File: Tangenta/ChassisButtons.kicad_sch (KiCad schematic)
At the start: 10 parts, among them J2 Conn_02x02_Top_Bottom, U5 74HC74D,653, U6 CD4060SA_TR, U7 74HC04D,653

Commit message: Current progress, power supply.
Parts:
- added Q1, Q2: 2N7002, NMOS_2N7002:NMOS_2N7002, symbol NMOS_2N7002:2N7002
- added R10, R6, R9: 100, Resistor_SMD:R_0603_1608Metric, symbol Device:R_Small_US
- added R7, R8: 10k, Resistor_SMD:R_0603_1608Metric, symbol Device:R_Small_US
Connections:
- net CONN_3: now also R6.1, R7.1
- net GNDREF: now also Q1.2 (S), Q2.2 (S), R7.2, R8.2
- net PS_ON: now also R10.1
- net CONN_4: now reaches U5.5 (1Q)
- net CONN_4: now also Q2.3 (D), R8.1, R9.1
- new net: Q2.1 (G), R6.2
- new net: Q1.3 (D), R10.2
- new net: Q1.1 (G), R9.2
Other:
- moved on the sheet: C1, J2, R1, R2, R3, R4, R5, U5, U6, U7

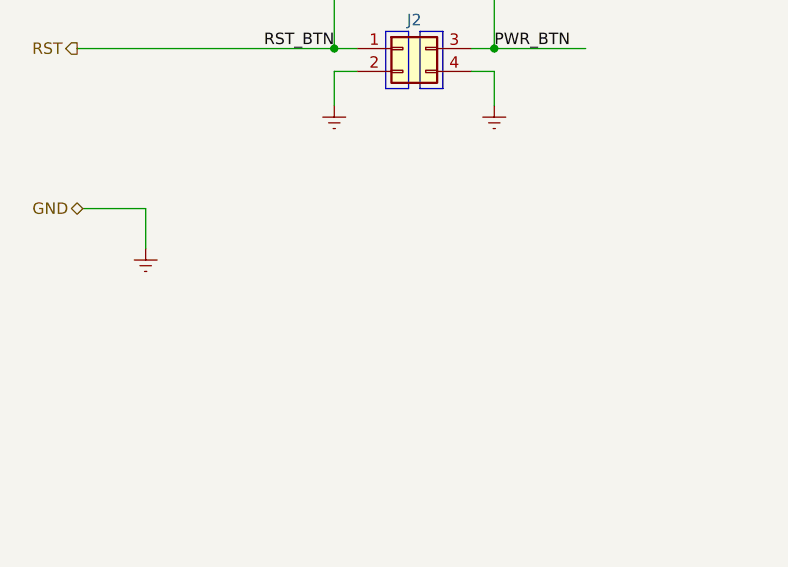
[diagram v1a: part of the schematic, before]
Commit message: Adding the TPS diode.
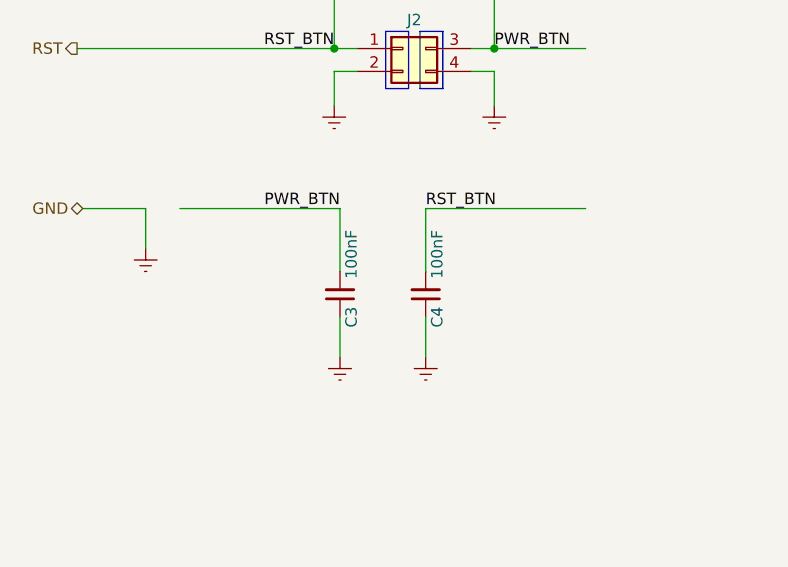
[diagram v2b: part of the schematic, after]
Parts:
- added C3, C4: 100nF, symbol Device:C_Small
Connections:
- net GNDREF: now also C3.1, C4.1
- net PWR_BTN: now also C3.2
- net RST: now also C4.2
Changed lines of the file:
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@@
+    (stroke (width 0) (type default))
+  )
+  (wire (pts (xy 69.215 113.665) (xy 69.215 118.11))
     (stroke (width 0) (type default))
   )
@@
     (stroke (width 0) (type default))
   )
+  (wire (pts (xy 96.52 101.6) (xy 78.74 101.6))
+    (stroke (width 0) (type default))
+  )
   (wire (pts (xy 68.58 90.17) (xy 68.58 86.36))
     (stroke (width 0) (type default))
@@
     (stroke (width 0) (type default))
   )
+  (wire (pts (xy 78.74 113.665) (xy 78.74 118.11))
+    (stroke (width 0) (type default))
+  )
   (wire (pts (xy 194.945 58.42) (xy 202.565 58.42))
     (stroke (width 0) (type default))
@@
     (stroke (width 0) (type default))
   )
+  (wire (pts (xy 78.74 101.6) (xy 78.74 108.585))
+    (stroke (width 0) (type default))
+  )
   (wire (pts (xy 226.695 102.235) (xy 226.695 116.205))
     (stroke (width 0) (type default))
@@
     (stroke (width 0) (type default))
   )
+  (wire (pts (xy 69.215 101.6) (xy 69.215 108.585))
+    (stroke (width 0) (type default))
+  )
   (wire (pts (xy 152.4 118.745) (xy 162.56 118.745))
     (stroke (width 0) (type default))
@@
     (stroke (width 0) (type default))
   )
+  (wire (pts (xy 51.435 101.6) (xy 69.215 101.6))
+    (stroke (width 0) (type default))
+  )
   (wire (pts (xy 211.455 131.445) (xy 211.455 137.16))
     (stroke (width 0) (type default))
@@
   )
   (label "CONN_3" (at 121.285 63.5 0) (fields_autoplaced)
+    (effects (font (size 1.27 1.27)) (justify left bottom))
+  )
+  (label "RST_BTN" (at 78.74 101.6 0) (fields_autoplaced)
     (effects (font (size 1.27 1.27)) (justify left bottom))
   )
@@
   )
   (label "ATX_GREEN_LINE" (at 67.945 55.88 180) (fields_autoplaced)
+    (effects (font (size 1.27 1.27)) (justify right bottom))
+  )
+  (label "PWR_BTN" (at 69.215 101.6 180) (fields_autoplaced)
     (effects (font (size 1.27 1.27)) (justify right bottom))
   )
@@
     )
   )
+  (symbol (lib_id "Device:C_Small") (at 69.215 111.125 0) (mirror x) (unit 1)
+    (in_bom yes) (on_board yes) (dnp no)
+    (property "Reference" "C3" (at 70.485 113.665 90)
+      (effects (font (size 1.27 1.27)))
+    )
+    (property "Value" "100nF" (at 70.485 106.68 90)
+      (effects (font (size 1.27 1.27)))
+    )
+    (property "Footprint" "" (at 69.215 111.125 0)
+      (effects (font (size 1.27 1.27)) hide)
+    )
+    (property "Datasheet" "~" (at 69.215 111.125 0)
+      (effects (font (size 1.27 1.27)) hide)
+    )
+    (pin "1")
+    (pin "2")
+    (instances
+      (project "Tangenta"
+        (path "/358d1bcf-7599-4352-8c4d-baa18a5f09e6/8215796b-9611-4f43-bcc5-319f8414b8a6"
+          (reference "C3") (unit 1)
+        )
+      )
+    )
+  )
   (symbol (lib_id "NMOS_2N7002:2N7002") (at 224.155 121.285 0) (unit 1)
     (in_bom yes) (on_board yes) (dnp no)
@@
     )
   )
+  (symbol (lib_id "power:GNDREF") (at 78.74 118.11 0) (unit 1)
+    (in_bom yes) (on_board yes) (dnp no) (fields_autoplaced)
+    (property "Reference" "#PWR011" (at 78.74 124.46 0)
+      (effects (font (size 1.27 1.27)) hide)
+    )
+    (property "Value" "GNDREF" (at 78.74 123.19 0)
+      (effects (font (size 1.27 1.27)) hide)
+    )
+    (property "Footprint" "" (at 78.74 118.11 0)
+      (effects (font (size 1.27 1.27)) hide)
+    )
+    (property "Datasheet" "" (at 78.74 118.11 0)
+      (effects (font (size 1.27 1.27)) hide)
+    )
+    (pin "1")
+    (instances
+      (project "Tangenta"
+        (path "/358d1bcf-7599-4352-8c4d-baa18a5f09e6/8215796b-9611-4f43-bcc5-319f8414b8a6"
+          (reference "#PWR011") (unit 1)
+        )
+      )
+    )
+  )
   (symbol (lib_id "power:GNDREF") (at 194.945 73.66 0) (unit 1)
     (in_bom yes) (on_board yes) (dnp no) (fields_autoplaced)
@@
     )
   )
+  (symbol (lib_id "Device:C_Small") (at 78.74 111.125 0) (mirror x) (unit 1)
+    (in_bom yes) (on_board yes) (dnp no)
+    (property "Reference" "C4" (at 80.01 113.665 90)
+      (effects (font (size 1.27 1.27)))
+    )
+    (property "Value" "100nF" (at 80.01 106.68 90)
+      (effects (font (size 1.27 1.27)))
+    )
+    (property "Footprint" "" (at 78.74 111.125 0)
+      (effects (font (size 1.27 1.27)) hide)
+    )
+    (property "Datasheet" "~" (at 78.74 111.125 0)
+      (effects (font (size 1.27 1.27)) hide)
+    )
+    (pin "1")
+    (pin "2")
+    (instances
+      (project "Tangenta"
+        (path "/358d1bcf-7599-4352-8c4d-baa18a5f09e6/8215796b-9611-4f43-bcc5-319f8414b8a6"
+          (reference "C4") (unit 1)
+        )
+      )
+    )
+  )
   (symbol (lib_id "power:GNDREF") (at 47.625 106.045 0) (unit 1)
     (in_bom yes) (on_board yes) (dnp no) (fields_autoplaced)
@@
         )
       )
+    )
+  )
+  (symbol (lib_id "power:GNDREF") (at 69.215 118.11 0) (unit 1)
+    (in_bom yes) (on_board yes) (dnp no) (fields_autoplaced)
+    (property "Reference" "#PWR012" (at 69.215 124.46 0)
+      (effects (font (size 1.27 1.27)) hide)
+    )
+    (property "Value" "GNDREF" (at 69.215 123.19 0)
+      (effects (font (size 1.27 1.27)) hide)
+    )
+    (property "Footprint" "" (at 69.215 118.11 0)
+      (effects (font (size 1.27 1.27)) hide)
+    )
+    (property "Datasheet" "" (at 69.215 118.11 0)
+      (effects (font (size 1.27 1.27)) hide)
+    )
+    (pin "1")
+    (instances
+      (project "Tangenta"
+        (path "/358d1bcf-7599-4352-8c4d-baa18a5f09e6/8215796b-9611-4f43-bcc5-319f8414b8a6"
+          (reference "#PWR012") (unit 1)
+        )
+      )

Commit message: Power supply - current progress.
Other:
- moved on the sheet: C1, R3, R4, U6
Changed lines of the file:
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@@
   (junction (at 68.58 68.58) (diameter 0) (color 0 0 0 0)
   )
-  (junction (at 177.165 116.205) (diameter 0) (color 0 0 0 0)
+  (junction (at 176.53 116.205) (diameter 0) (color 0 0 0 0)
   )
   (junction (at 211.455 121.285) (diameter 0) (color 0 0 0 0)
@@
     (stroke (width 0) (type default))
   )
-  (wire (pts (xy 152.4 116.205) (xy 166.37 116.205))
+  (wire (pts (xy 151.765 116.205) (xy 165.735 116.205))
     (stroke (width 0) (type default))
   )
@@
     (stroke (width 0) (type default))
   )
-  (wire (pts (xy 152.4 100.965) (xy 160.655 100.965))
+  (wire (pts (xy 151.765 100.965) (xy 160.02 100.965))
     (stroke (width 0) (type default))
   )
@@
     (stroke (width 0) (type default))
   )
-  (wire (pts (xy 152.4 111.125) (xy 160.655 111.125))
+  (wire (pts (xy 151.765 111.125) (xy 160.02 111.125))
     (stroke (width 0) (type default))
   )
@@
     (stroke (width 0) (type default))
   )
-  (wire (pts (xy 152.4 108.585) (xy 160.655 108.585))
-    (stroke (width 0) (type default))
-  )
-  (wire (pts (xy 177.165 111.76) (xy 177.165 116.205))
+  (wire (pts (xy 151.765 108.585) (xy 160.02 108.585))
+    (stroke (width 0) (type default))
+  )
+  (wire (pts (xy 176.53 111.76) (xy 176.53 116.205))
     (stroke (width 0) (type default))
   )
@@
     (stroke (width 0) (type default))
   )
-  (wire (pts (xy 162.56 120.65) (xy 166.37 120.65))
+  (wire (pts (xy 161.925 120.65) (xy 165.735 120.65))
     (stroke (width 0) (type default))
   )
@@
     (stroke (width 0) (type default))
   )
-  (wire (pts (xy 177.165 120.65) (xy 171.45 120.65))
-    (stroke (width 0) (type default))
-  )
-  (wire (pts (xy 124.46 118.745) (xy 132.08 118.745))
+  (wire (pts (xy 176.53 120.65) (xy 170.815 120.65))
+    (stroke (width 0) (type default))
+  )
+  (wire (pts (xy 123.825 118.745) (xy 131.445 118.745))
     (stroke (width 0) (type default))
   )
@@
     (stroke (width 0) (type default))
   )
-  (wire (pts (xy 152.4 113.665) (xy 162.56 113.665))
+  (wire (pts (xy 151.765 113.665) (xy 161.925 113.665))
     (stroke (width 0) (type default))
   )
@@
     (stroke (width 0) (type default))
   )
-  (wire (pts (xy 162.56 118.745) (xy 162.56 120.65))
-    (stroke (width 0) (type default))
-  )
-  (wire (pts (xy 171.45 116.205) (xy 177.165 116.205))
+  (wire (pts (xy 161.925 118.745) (xy 161.925 120.65))
+    (stroke (width 0) (type default))
+  )
+  (wire (pts (xy 170.815 116.205) (xy 176.53 116.205))
     (stroke (width 0) (type default))
   )
@@
     (stroke (width 0) (type default))
   )
-  (wire (pts (xy 171.45 111.76) (xy 177.165 111.76))
+  (wire (pts (xy 170.815 111.76) (xy 176.53 111.76))
     (stroke (width 0) (type default))
   )
@@
     (stroke (width 0) (type default))
   )
-  (wire (pts (xy 152.4 118.745) (xy 162.56 118.745))
-    (stroke (width 0) (type default))
-  )
-  (wire (pts (xy 177.165 116.205) (xy 177.165 120.65))
-    (stroke (width 0) (type default))
-  )
-  (wire (pts (xy 162.56 113.665) (xy 162.56 111.76))
+  (wire (pts (xy 151.765 118.745) (xy 161.925 118.745))
+    (stroke (width 0) (type default))
+  )
+  (wire (pts (xy 176.53 116.205) (xy 176.53 120.65))
+    (stroke (width 0) (type default))
+  )
+  (wire (pts (xy 161.925 113.665) (xy 161.925 111.76))
     (stroke (width 0) (type default))
   )
@@
     (stroke (width 0) (type default))
   )
-  (wire (pts (xy 162.56 111.76) (xy 166.37 111.76))
+  (wire (pts (xy 161.925 111.76) (xy 165.735 111.76))
     (stroke (width 0) (type default))
   )
@@
     (effects (font (size 1.27 1.27)) (justify right bottom))
   )
-  (label "PWR_BTN" (at 152.4 111.125 0) (fields_autoplaced)
+  (label "PWR_BTN" (at 151.765 111.125 0) (fields_autoplaced)
     (effects (font (size 1.27 1.27)) (justify left bottom))
   )
@@
     (effects (font (size 1.27 1.27)) (justify left bottom))
   )
-  (label "VCC_LOGIC" (at 152.4 100.965 0) (fields_autoplaced)
+  (label "VCC_LOGIC" (at 151.765 100.965 0) (fields_autoplaced)
     (effects (font (size 1.27 1.27)) (justify left bottom))
   )
@@
     (effects (font (size 1.27 1.27)) (justify left bottom))
   )
-  (label "CONN_3" (at 153.67 108.585 0) (fields_autoplaced)
+  (label "CONN_3" (at 153.035 108.585 0) (fields_autoplaced)
     (effects (font (size 1.27 1.27)) (justify left bottom))
   )
@@
     )
   )
-  (symbol (lib_id "Device:R_Small_US") (at 168.91 116.205 90) (unit 1)
-    (in_bom yes) (on_board yes) (dnp no)
-    (property "Reference" "R3" (at 166.37 114.935 90)
-      (effects (font (size 1.27 1.27)))
-    )
-    (property "Value" "100k" (at 172.72 114.935 90)
-      (effects (font (size 1.27 1.27)))
-    )
-    (property "Footprint" "Resistor_SMD:R_0603_1608Metric" (at 168.91 116.205 0)
-      (effects (font (size 1.27 1.27)) hide)
-    )
-    (property "Datasheet" "~" (at 168.91 116.205 0)
+  (symbol (lib_id "Device:R_Small_US") (at 168.275 116.205 90) (unit 1)
+    (in_bom yes) (on_board yes) (dnp no)
+    (property "Reference" "R3" (at 165.735 114.935 90)
+      (effects (font (size 1.27 1.27)))
+    )
+    (property "Value" "100k" (at 172.085 114.935 90)
+      (effects (font (size 1.27 1.27)))
+    )
+    (property "Footprint" "Resistor_SMD:R_0603_1608Metric" (at 168.275 116.205 0)
+      (effects (font (size 1.27 1.27)) hide)
+    )
+    (property "Datasheet" "~" (at 168.275 116.205 0)
       (effects (font (size 1.27 1.27)) hide)
     )
@@
     )
   )
-  (symbol (lib_id "CD4060:CD4060SA_TR") (at 142.24 109.855 0) (unit 1)
-    (in_bom yes) (on_board yes) (dnp no)
-    (property "Reference" "U6" (at 135.89 97.155 0)
-      (effects (font (size 1.27 1.27)))
-    )
-    (property "Value" "CD4060SA_TR" (at 142.24 122.555 0)
-      (effects (font (size 1.27 1.27)))
-    )
-    (property "Footprint" "CD4060:CD4060" (at 142.24 128.524 0)
+  (symbol (lib_id "CD4060:CD4060SA_TR") (at 141.605 109.855 0) (unit 1)
+    (in_bom yes) (on_board yes) (dnp no)
+    (property "Reference" "U6" (at 135.255 97.155 0)
+      (effects (font (size 1.27 1.27)))
+    )
+    (property "Value" "CD4060SA_TR" (at 141.605 122.555 0)
+      (effects (font (size 1.27 1.27)))
+    )
+    (property "Footprint" "CD4060:CD4060" (at 141.605 128.524 0)
       (effects (font (size 1.27 1.27) italic) hide)
     )
-    (property "Datasheet" "http://datasheet.octopart.com/MC14076BDR2G-ON-Semiconductor-datasheet-608107.pdf" (at 134.874 130.81 0)
+    (property "Datasheet" "http://datasheet.octopart.com/MC14076BDR2G-ON-Semiconductor-datasheet-608107.pdf" (at 134.239 130.81 0)
       (effects (font (size 1.27 1.27)) (justify left) hide)
     )
-    (property "LCSC" "C2943323" (at 139.446 126.238 0)
+    (property "LCSC" "C2943323" (at 138.811 126.238 0)
       (effects (font (size 1.27 1.27)) hide)
     )
@@
     )
   )
-  (symbol (lib_id "Device:R_Small_US") (at 168.91 111.76 90) (unit 1)
-    (in_bom yes) (on_board yes) (dnp no)
-    (property "Reference" "R4" (at 166.37 110.49 90)
-      (effects (font (size 1.27 1.27)))
-    )
-    (property "Value" "1k" (at 171.45 110.49 90)
-      (effects (font (size 1.27 1.27)))
-    )
-    (property "Footprint" "Resistor_SMD:R_0603_1608Metric" (at 168.91 111.76 0)
-      (effects (font (size 1.27 1.27)) hide)
-    )
-    (property "Datasheet" "~" (at 168.91 111.76 0)
+  (symbol (lib_id "Device:R_Small_US") (at 168.275 111.76 90) (unit 1)
+    (in_bom yes) (on_board yes) (dnp no)
+    (property "Reference" "R4" (at 165.735 110.49 90)
+      (effects (font (size 1.27 1.27)))
+    )
+    (property "Value" "1k" (at 170.815 110.49 90)
+      (effects (font (size 1.27 1.27)))
+    )
+    (property "Footprint" "Resistor_SMD:R_0603_1608Metric" (at 168.275 111.76 0)
+      (effects (font (size 1.27 1.27)) hide)
+    )
+    (property "Datasheet" "~" (at 168.275 111.76 0)
       (effects (font (size 1.27 1.27)) hide)
     )
@@
     )
   )
-  (symbol (lib_id "Device:C_Small") (at 168.91 120.65 90) (unit 1)
-    (in_bom yes) (on_board yes) (dnp no)
-    (property "Reference" "C1" (at 166.37 119.38 90)
-      (effects (font (size 1.27 1.27)))
-    )
-    (property "Value" "100nF" (at 173.355 119.38 90)
-      (effects (font (size 1.27 1.27)))
-    )
-    (property "Footprint" "" (at 168.91 120.65 0)
-      (effects (font (size 1.27 1.27)) hide)
-    )
-    (property "Datasheet" "~" (at 168.91 120.65 0)
+  (symbol (lib_id "Device:C_Small") (at 168.275 120.65 90) (unit 1)
+    (in_bom yes) (on_board yes) (dnp no)
+    (property "Reference" "C1" (at 165.735 119.38 90)
+      (effects (font (size 1.27 1.27)))
+    )
+    (property "Value" "100nF" (at 172.72 119.38 90)
+      (effects (font (size 1.27 1.27)))
+    )
+    (property "Footprint" "" (at 168.275 120.65 0)
+      (effects (font (size 1.27 1.27)) hide)
+    )
+    (property "Datasheet" "~" (at 168.275 120.65 0)
       (effects (font (size 1.27 1.27)) hide)
     )
@@
     )
   )
-  (symbol (lib_id "power:GNDREF") (at 124.46 118.745 0) (unit 1)
-    (in_bom yes) (on_board yes) (dnp no) (fields_autoplaced)
-    (property "Reference" "#PWR06" (at 124.46 125.095 0)
-      (effects (font (size 1.27 1.27)) hide)
-    )
-    (property "Value" "GNDREF" (at 124.46 123.825 0)
-      (effects (font (size 1.27 1.27)) hide)
-    )
-    (property "Footprint" "" (at 124.46 118.745 0)
-      (effects (font (size 1.27 1.27)) hide)
-    )
-    (property "Datasheet" "" (at 124.46 118.745 0)
-      (effects (font (size 1.27 1.27)) hide)
-    )
+  (symbol (lib_id "power:GNDREF") (at 123.825 118.745 0) (unit 1)
+    (in_bom yes) (on_board yes) (dnp no) (fields_autoplaced)
+    (property "Reference" "#PWR06" (at 123.825 125.095 0)
+      (effects (font (size 1.27 1.27)) hide)
+    )
+    (property "Value" "GNDREF" (at 123.825 123.825 0)
+      (effects (font (size 1.27 1.27)) hide)
+    )
+    (property "Footprint" "" (at 123.825 118.745 0)
+      (effects (font (size 1.27 1.27)) hide)
+    )
+    (property "Datasheet" "" (at 123.825 118.745 0)
+      (effects (font (size 1.27 1.27)) hide)
+    )

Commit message: Current progress...
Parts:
- C1, C3, C4: footprint (none) -> Capacitor_SMD:C_0603_1608Metric
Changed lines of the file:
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@@
       (effects (font (size 1.27 1.27)))
     )
-    (property "Footprint" "" (at 69.215 111.125 0)
+    (property "Footprint" "Capacitor_SMD:C_0603_1608Metric" (at 69.215 111.125 0)
       (effects (font (size 1.27 1.27)) hide)
     )
@@
       (effects (font (size 1.27 1.27)))
     )
-    (property "Footprint" "" (at 168.275 120.65 0)
+    (property "Footprint" "Capacitor_SMD:C_0603_1608Metric" (at 168.275 120.65 0)
       (effects (font (size 1.27 1.27)) hide)
     )
@@
       (effects (font (size 1.27 1.27)))
     )
-    (property "Footprint" "" (at 78.74 111.125 0)
-      (effects (font (size 1.27 1.27)) hide)
-    )
+    (property "Footprint" "Capacitor_SMD:C_0603_1608Metric" (at 78.74 111.125 0)
+      (effects (font (size 1.27 1.27)) hide)
+    )

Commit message: Current progress...
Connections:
- net PWR_BTN renamed PWR
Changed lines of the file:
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@@
     (effects (font (size 1.27 1.27)) (justify left bottom))
+  )
+  (hierarchical_label "PWR" (shape output) (at 96.52 83.82 0) (fields_autoplaced)
+    (effects (font (size 1.27 1.27)) (justify left))
   )
   (hierarchical_label "GND" (shape bidirectional) (at 40.64 101.6 180) (fields_autoplaced)
